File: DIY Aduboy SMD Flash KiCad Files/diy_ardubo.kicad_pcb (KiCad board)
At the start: 2 copper layers, 79.5 x 88 mm, 27 parts, among them J1 Batt. Connector, J2 Conn_01x07_Pin, Q1 BC557, SW5 SW_Push, SW6 SW_Push, U1 ProMicro, U2 W25Q128JVS

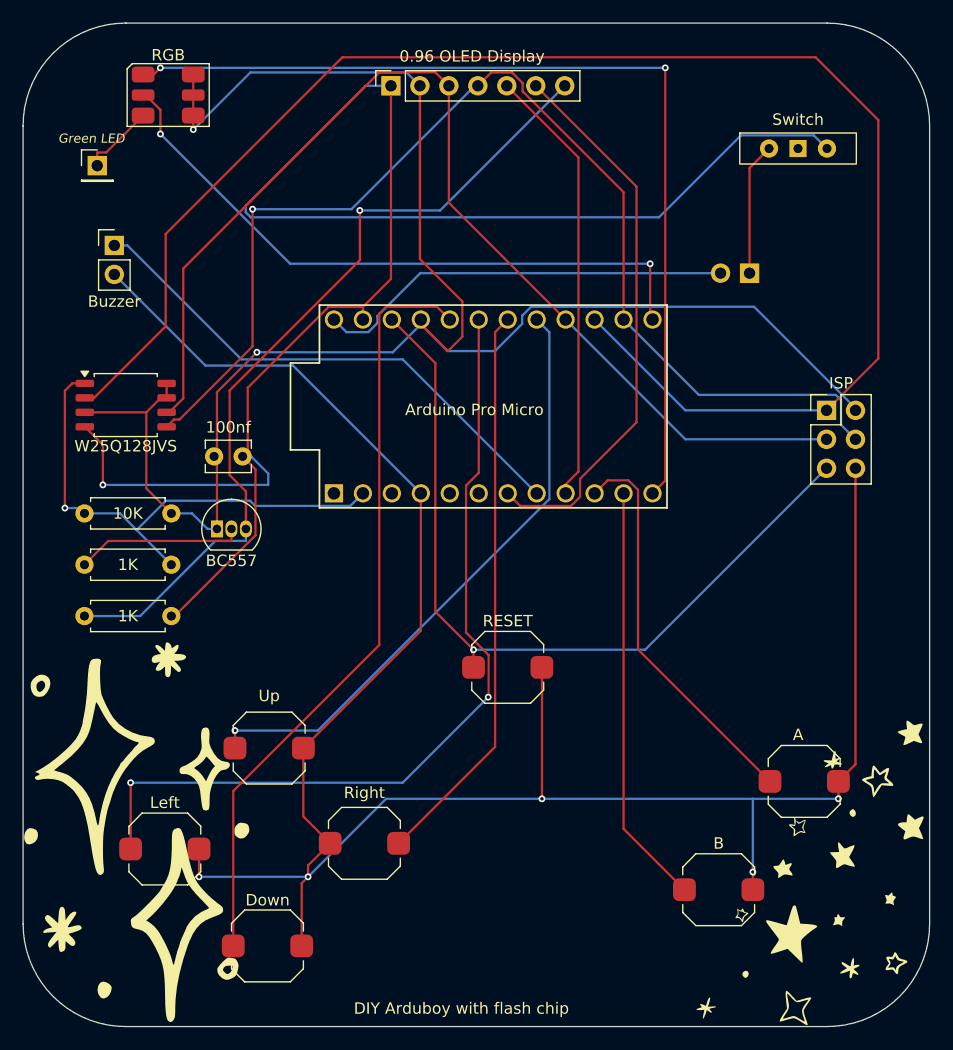
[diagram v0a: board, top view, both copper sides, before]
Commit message: Updated Schematics
Fixed ground pin issue with switch
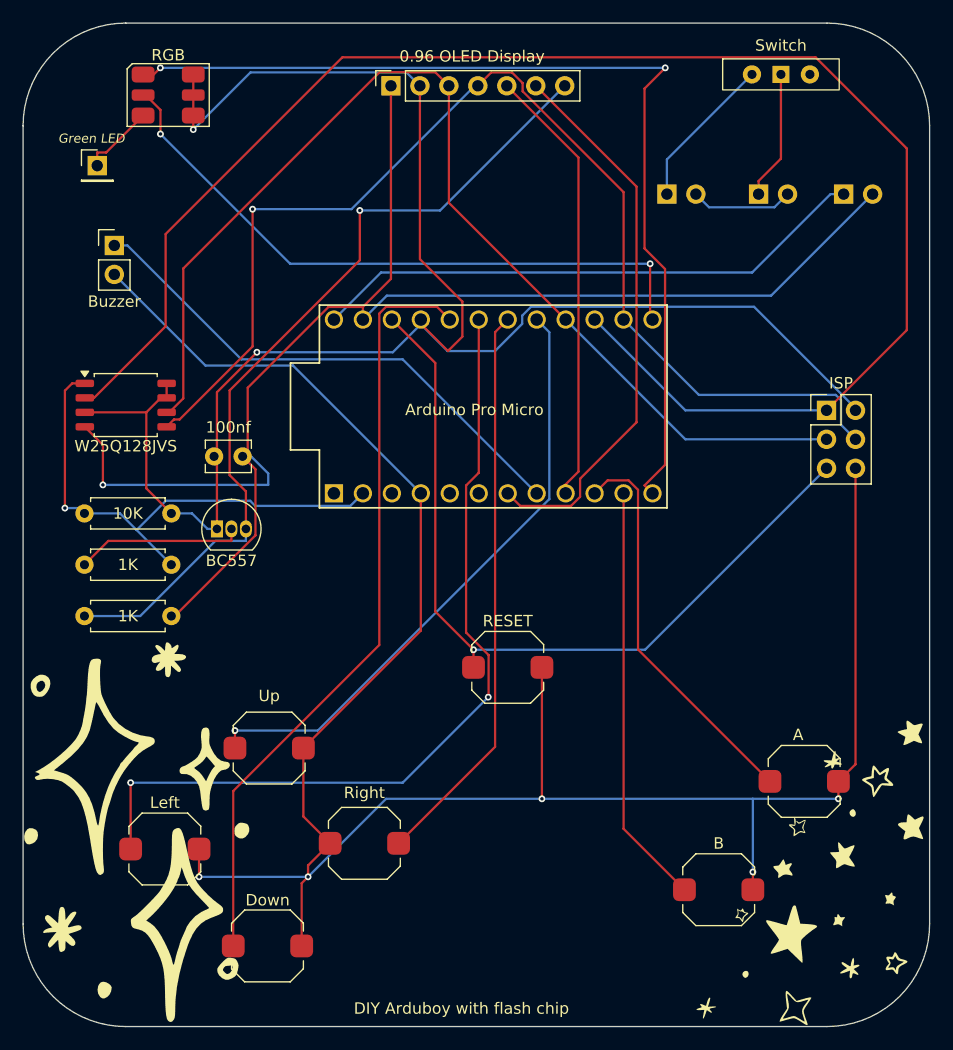
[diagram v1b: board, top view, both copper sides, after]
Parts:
- removed J1: Batt. Connector, Connector_PinHeader_2.54mm:PinHeader_2x01_P2.54mm_Vertical
- added BOOSTER IN: Conn_01x02_Pin, Connector_PinHeader_2.54mm:PinHeader_1x02_P2.54mm_Vertical, B.Cu at (178.5, 63.5)
- added BOOSTER OUT: Conn_01x02_Pin, Connector_PinHeader_2.54mm:PinHeader_1x02_P2.54mm_Vertical, B.Cu at (194.0, 63.5)
- added TP4056 IN: Conn_01x02_Pin, Connector_PinHeader_2.54mm:PinHeader_1x02_P2.54mm_Vertical, B.Cu at (186.5, 63.5)
- R1: value R2 -> R
- R2: value R3 -> R
- moved Switch 6.67 mm to (188.5, 53.0)
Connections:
- Switch pad 1: unconnected-(SW8-A-Pad1) -> Net-(J5-Pin_1)
- Switch pad 3: Net-(J2-GND) -> unconnected-(SW8-C-Pad3)
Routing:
- net Net-(J2-GND): track 155.1 -> 132.1 mm
- net Net-(J6-Pin_1): track 36.9 -> 49.3 mm
- net Net-(J5-Pin_1): track 0.00 -> 11.3 mm
- net Net-(J1-Pin_2): track 0.00 -> 8.99 mm
- net Net-(D2-KB): track 83.8 -> 85.9 mm
- net Net-(J1-Pin_1): track 11.6 -> 13.6 mm
- net Net-(J3-Pin_1): track 140.4 -> 141.5 mm
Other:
- board text added: "+"
- board text added: "-"
